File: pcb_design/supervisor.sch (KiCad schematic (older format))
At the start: 17 parts, among them U5 7400-TSSOP, U6 SN74ALVC08PWR, U7 SN74ALVC08PWR, U8 SN74AUP1G74

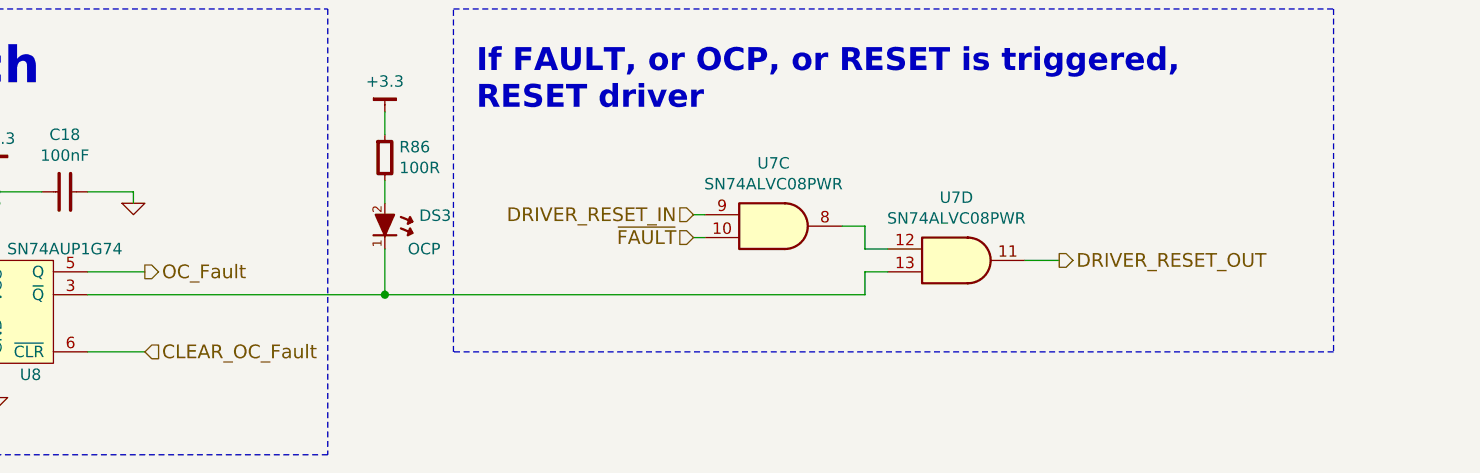
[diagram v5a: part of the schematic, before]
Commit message: Fixed issue with non-bidirectional phase current measurement. Started routing power supplies. Changed terminal blocks from 5.00mm to 3.81mm pitch
Signed-off-by: Marcos Chaparro <mchaparro@paltatech.com>
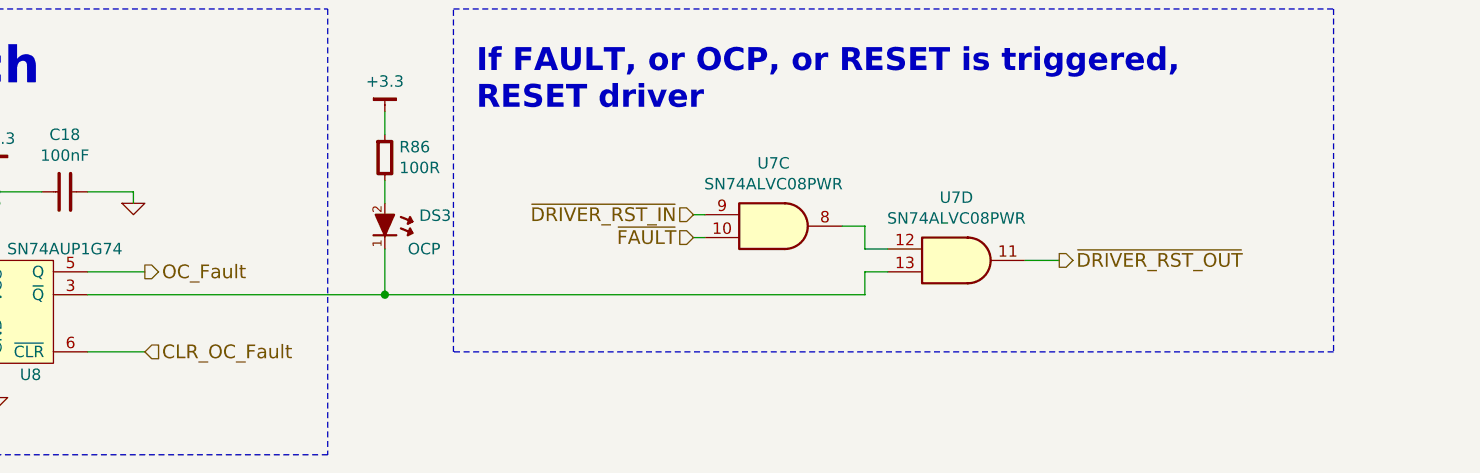
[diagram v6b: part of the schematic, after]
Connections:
- net CLEAR_OC_Fault renamed CLR_OC_Fault
- net DRIVER_RESET_IN renamed ~DRIVER_RST_IN
- net DRIVER_RESET_OUT renamed ~DRIVER_RST_OUT
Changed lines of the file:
@@
 encoding utf-8
 Sheet 7 13
-Title ""
-Date ""
-Rev ""
-Comp ""
+Title "Monitor logic"
+Date "2017-01-24"
+Rev "0.1"
+Comp "vedder.se + PALTA TECH S.A. + PYMCO.fr"
 Comment1 ""
 Comment2 ""
@@
 $EndDescr
 Text HLabel 8450 6550 2    60   Output ~ 0
-DRIVER_RESET_OUT
+~DRIVER_RST_OUT
 Text HLabel 1550 1950 0    60   Input ~ 0
 PWM_UT
@@
 Connection ~ 2000 2050
 $Comp
-L GND #PWR83
+L GND #PWR086
 U 1 1 588831C2
 P 1850 2400
-F 0 "#PWR83" H 1850 2400 30  0001 C CNN
+F 0 "#PWR086" H 1850 2400 30  0001 C CNN
 F 1 "GND" H 1850 2330 30  0001 C CNN
 F 2 "" H 1850 2400 60  0000 C CNN
@@
 	1850 2400 1850 2350
 $Comp
-L GND #PWR86
+L GND #PWR087
 U 1 1 58883201
 P 2000 2400
-F 0 "#PWR86" H 2000 2400 30  0001 C CNN
+F 0 "#PWR087" H 2000 2400 30  0001 C CNN
 F 1 "GND" H 2000 2330 30  0001 C CNN
 F 2 "" H 2000 2400 60  0000 C CNN
@@
 Connection ~ 2000 3300
 $Comp
-L GND #PWR84
+L GND #PWR088
 U 1 1 588824FD
 P 1850 3650
-F 0 "#PWR84" H 1850 3650 30  0001 C CNN
+F 0 "#PWR088" H 1850 3650 30  0001 C CNN
 F 1 "GND" H 1850 3580 30  0001 C CNN
 F 2 "" H 1850 3650 60  0000 C CNN
@@
 	1850 3650 1850 3600
 $Comp
-L GND #PWR87
+L GND #PWR089
 U 1 1 58882504
 P 2000 3650
-F 0 "#PWR87" H 2000 3650 30  0001 C CNN
+F 0 "#PWR089" H 2000 3650 30  0001 C CNN
 F 1 "GND" H 2000 3580 30  0001 C CNN
 F 2 "" H 2000 3650 60  0000 C CNN
@@
 Connection ~ 2000 4550
 $Comp
-L GND #PWR85
+L GND #PWR090
 U 1 1 5888288C
 P 1850 4900
-F 0 "#PWR85" H 1850 4900 30  0001 C CNN
+F 0 "#PWR090" H 1850 4900 30  0001 C CNN
 F 1 "GND" H 1850 4830 30  0001 C CNN
 F 2 "" H 1850 4900 60  0000 C CNN
@@
 	1850 4900 1850 4850
 $Comp
-L GND #PWR88
+L GND #PWR091
 U 1 1 58882893
 P 2000 4900
-F 0 "#PWR88" H 2000 4900 30  0001 C CNN
+F 0 "#PWR091" H 2000 4900 30  0001 C CNN
 F 1 "GND" H 2000 4830 30  0001 C CNN
 F 2 "" H 2000 4900 60  0000 C CNN
@@
 $EndComp
 $Comp
-L GND #PWR91
+L GND #PWR092
 U 1 1 5888A11E
 P 3800 7150
-F 0 "#PWR91" H 3800 7150 30  0001 C CNN
+F 0 "#PWR092" H 3800 7150 30  0001 C CNN
 F 1 "GND" H 3800 7080 30  0001 C CNN
 F 2 "" H 3800 7150 60  0000 C CNN
@@
 	4400 6250 4400 6300
 $Comp
-L GND #PWR92
+L GND #PWR093
 U 1 1 5888A46C
 P 4400 6300
-F 0 "#PWR92" H 4400 6300 30  0001 C CNN
+F 0 "#PWR093" H 4400 6300 30  0001 C CNN
 F 1 "GND" H 4400 6230 30  0001 C CNN
 F 2 "" H 4400 6300 60  0000 C CNN
@@
 	4450 6600 4200 6600
 Text HLabel 4450 6950 2    60   Input ~ 0
-CLEAR_OC_Fault
+CLR_OC_Fault
 Wire Wire Line
 	4450 6950 4200 6950
@@
 	8450 6550 8300 6550
 Text HLabel 6850 6350 0    60   Input ~ 0
-DRIVER_RESET_IN
+~DRIVER_RST_IN
 Wire Wire Line
 	6850 6350 6900 6350
@@
 	5600 4950 5600 5050
 $Comp
-L GND #PWR99
+L GND #PWR094
 U 1 1 58899228
 P 5600 5050
-F 0 "#PWR99" H 5600 5050 30  0001 C CNN
+F 0 "#PWR094" H 5600 5050 30  0001 C CNN
 F 1 "GND" H 5600 4980 30  0001 C CNN
 F 2 "" H 5600 5050 60  0000 C CNN
@@
 Connection ~ 5600 5000
 $Comp
-L GND #PWR97
+L GND #PWR095
 U 1 1 5889937C
 P 5600 3700
-F 0 "#PWR97" H 5600 3700 30  0001 C CNN
+F 0 "#PWR095" H 5600 3700 30  0001 C CNN
 F 1 "GND" H 5600 3630 30  0001 C CNN
 F 2 "" H 5600 3700 60  0000 C CNN
@@
 $EndComp
 $Comp
-L GND #PWR95
+L GND #PWR096
 U 1 1 588993D2
 P 5600 2450
-F 0 "#PWR95" H 5600 2450 30  0001 C CNN
+F 0 "#PWR096" H 5600 2450 30  0001 C CNN
 F 1 "GND" H 5600 2380 30  0001 C CNN
 F 2 "" H 5600 2450 60  0000 C CNN
@@
 	5500 5900 5500 6000
 $Comp
-L +3.3 #PWR98
+L +3.3 #PWR097
 U 1 1 588B453A
 P 5600 4050
-F 0 "#PWR98" H 5650 4100 30  0001 C CNN
+F 0 "#PWR097" H 5650 4100 30  0001 C CNN
 F 1 "+3.3" H 5600 4183 50  0000 C CNN
 F 2 "" H -950 100 60  0000 C CNN
@@
 $EndComp
 $Comp
-L +3.3 #PWR96
+L +3.3 #PWR098
 U 1 1 588B46D1
 P 5600 2700
-F 0 "#PWR96" H 5650 2750 30  0001 C CNN
+F 0 "#PWR098" H 5650 2750 30  0001 C CNN
 F 1 "+3.3" H 5600 2833 50  0000 C CNN
 F 2 "" H -950 -1250 60  0000 C CNN
@@
 $EndComp
 $Comp
-L +3.3 #PWR94
+L +3.3 #PWR099
 U 1 1 588B47E2
 P 5600 1450
-F 0 "#PWR94" H 5650 1500 30  0001 C CNN
+F 0 "#PWR099" H 5650 1500 30  0001 C CNN
 F 1 "+3.3" H 5600 1583 50  0000 C CNN
 F 2 "" H -950 -2500 60  0000 C CNN
@@
 $EndComp
 $Comp
-L +3.3 #PWR93
+L +3.3 #PWR0100
 U 1 1 588B4A14
 P 5500 5900
-F 0 "#PWR93" H 5550 5950 30  0001 C CNN
+F 0 "#PWR0100" H 5550 5950 30  0001 C CNN
 F 1 "+3.3" H 5500 6033 50  0000 C CNN
 F 2 "" H -1050 1950 60  0000 C CNN
@@
 $EndComp
 $Comp
-L +3.3 #PWR90
+L +3.3 #PWR0101
 U 1 1 588B4BFB
 P 3800 6150
-F 0 "#PWR90" H 3850 6200 30  0001 C CNN
+F 0 "#PWR0101" H 3850 6200 30  0001 C CNN
 F 1 "+3.3" H 3800 6283 50  0000 C CNN
 F 2 "" H -2750 2200 60  0000 C CNN
@@
 $EndComp
 $Comp
-L +3.3 #PWR89
+L +3.3 #PWR0102
 U 1 1 588B4CB5
 P 2050 6350
-F 0 "#PWR89" H 2100 6400 30  0001 C CNN
+F 0 "#PWR0102" H 2100 6400 30  0001 C CNN
 F 1 "+3.3" H 2050 6483 50  0000 C CNN
 F 2 "" H -4500 2400 60  0000 C CNN
